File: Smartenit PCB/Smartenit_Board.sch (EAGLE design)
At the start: 86 parts, among them J1 2X5CONNECTOR1.27MM, Q1 QUARTZ_3.58M_2PIN, U1 SN74LVC1G3157, U2 ADE7953, U3 ESP-WROOM-32

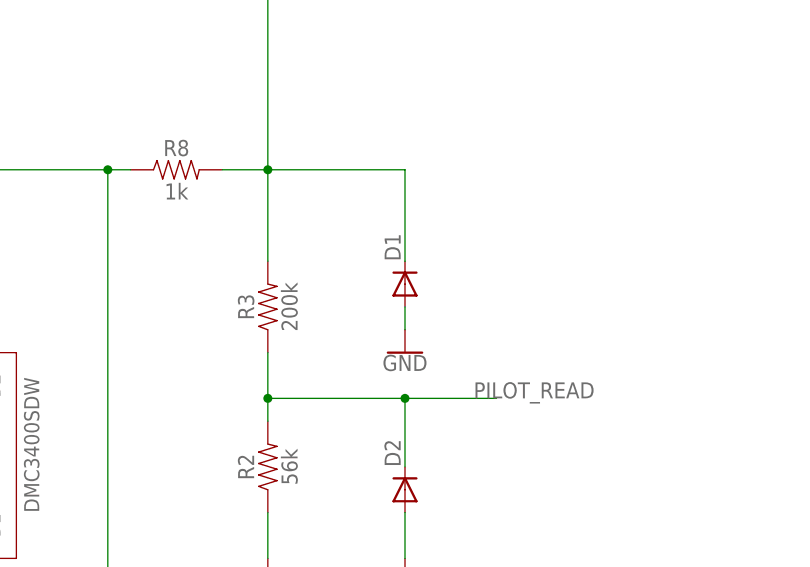
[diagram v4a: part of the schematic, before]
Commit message: fixed diodes
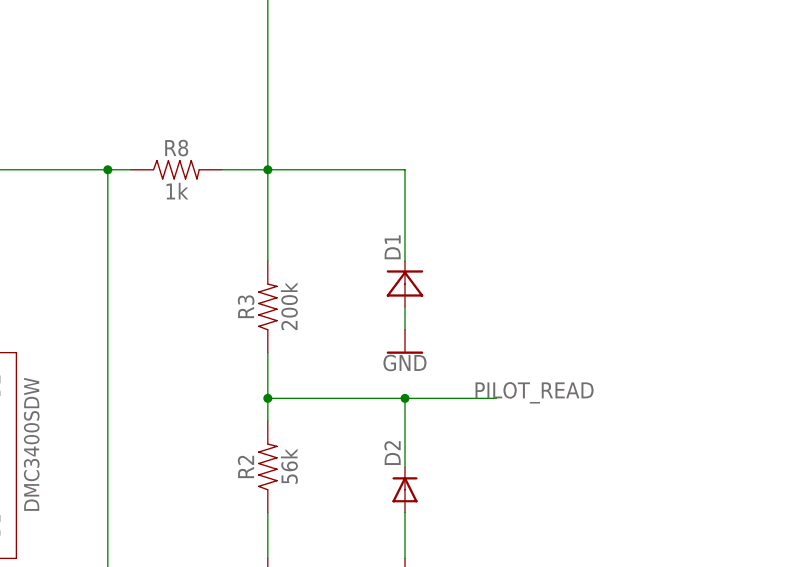
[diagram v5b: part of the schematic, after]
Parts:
- D1: device diode:DIODE-SMB -> Smart_Charger:TVSDIODE
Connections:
- net DGND: now also D1.P; no longer D1.A
- net PILOT: now also D1.N; no longer D1.C
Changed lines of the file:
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@@
 <grid distance="0.1" unitdist="inch" unit="inch" style="lines" multiple="1" display="no" altdistance="0.01" altunitdist="inch" altunit="inch"/>
 <layers>
-<layer number="1" name="Top" color="4" fill="1" visible="no" active="no"/>
-<layer number="2" name="Route2" color="1" fill="3" visible="no" active="no"/>
-<layer number="3" name="Route3" color="4" fill="3" visible="no" active="no"/>
-<layer number="4" name="Route4" color="1" fill="4" visible="no" active="no"/>
-<layer number="5" name="Route5" color="4" fill="4" visible="no" active="no"/>
-<layer number="6" name="Route6" color="1" fill="8" visible="no" active="no"/>
-<layer number="7" name="Route7" color="4" fill="8" visible="no" active="no"/>
-<layer number="8" name="Route8" color="1" fill="2" visible="no" active="no"/>
-<layer number="9" name="Route9" color="4" fill="2" visible="no" active="no"/>
-<layer number="10" name="Route10" color="1" fill="7" visible="no" active="no"/>
-<layer number="11" name="Route11" color="4" fill="7" visible="no" active="no"/>
-<layer number="12" name="Route12" color="1" fill="5" visible="no" active="no"/>
-<layer number="13" name="Route13" color="4" fill="5" visible="no" active="no"/>
-<layer number="14" name="Route14" color="1" fill="6" visible="no" active="no"/>
-<layer number="15" name="Route15" color="4" fill="6" visible="no" active="no"/>
-<layer number="16" name="Bottom" color="1" fill="1" visible="no" active="no"/>
-<layer number="17" name="Pads" color="2" fill="1" visible="no" active="no"/>
-<layer number="18" name="Vias" color="2" fill="1" visible="no" active="no"/>
-<layer number="19" name="Unrouted" color="6" fill="1" visible="no" active="no"/>
-<layer number="20" name="Dimension" color="15" fill="1" visible="no" active="no"/>
-<layer number="21" name="tPlace" color="7" fill="1" visible="no" active="no"/>
-<layer number="22" name="bPlace" color="7" fill="1" visible="no" active="no"/>
-<layer number="23" name="tOrigins" color="15" fill="1" visible="no" active="no"/>
-<layer number="24" name="bOrigins" color="15" fill="1" visible="no" active="no"/>
-<layer number="25" name="tNames" color="7" fill="1" visible="no" active="no"/>
-<layer number="26" name="bNames" color="7" fill="1" visible="no" active="no"/>
-<layer number="27" name="tValues" color="7" fill="1" visible="no" active="no"/>
-<layer number="28" name="bValues" color="7" fill="1" visible="no" active="no"/>
+<layer number="1" name="Top" color="4" fill="1" visible="yes" active="no"/>
+<layer number="2" name="Route2" color="1" fill="3" visible="yes" active="no"/>
+<layer number="3" name="Route3" color="4" fill="3" visible="yes" active="no"/>
+<layer number="4" name="Route4" color="1" fill="4" visible="yes" active="no"/>
+<layer number="5" name="Route5" color="4" fill="4" visible="yes" active="no"/>
+<layer number="6" name="Route6" color="1" fill="8" visible="yes" active="no"/>
+<layer number="7" name="Route7" color="4" fill="8" visible="yes" active="no"/>
+<layer number="8" name="Route8" color="1" fill="2" visible="yes" active="no"/>
+<layer number="9" name="Route9" color="4" fill="2" visible="yes" active="no"/>
+<layer number="10" name="Route10" color="1" fill="7" visible="yes" active="no"/>
+<layer number="11" name="Route11" color="4" fill="7" visible="yes" active="no"/>
+<layer number="12" name="Route12" color="1" fill="5" visible="yes" active="no"/>
+<layer number="13" name="Route13" color="4" fill="5" visible="yes" active="no"/>
+<layer number="14" name="Route14" color="1" fill="6" visible="yes" active="no"/>
+<layer number="15" name="Route15" color="4" fill="6" visible="yes" active="no"/>
+<layer number="16" name="Bottom" color="1" fill="1" visible="yes" active="no"/>
+<layer number="17" name="Pads" color="2" fill="1" visible="yes" active="no"/>
+<layer number="18" name="Vias" color="2" fill="1" visible="yes" active="no"/>
+<layer number="19" name="Unrouted" color="6" fill="1" visible="yes" active="no"/>
+<layer number="20" name="Dimension" color="15" fill="1" visible="yes" active="no"/>
+<layer number="21" name="tPlace" color="7" fill="1" visible="yes" active="no"/>
+<layer number="22" name="bPlace" color="7" fill="1" visible="yes" active="no"/>
+<layer number="23" name="tOrigins" color="15" fill="1" visible="yes" active="no"/>
+<layer number="24" name="bOrigins" color="15" fill="1" visible="yes" active="no"/>
+<layer number="25" name="tNames" color="7" fill="1" visible="yes" active="no"/>
+<layer number="26" name="bNames" color="7" fill="1" visible="yes" active="no"/>
+<layer number="27" name="tValues" color="7" fill="1" visible="yes" active="no"/>
+<layer number="28" name="bValues" color="7" fill="1" visible="yes" active="no"/>
 <layer number="29" name="tStop" color="7" fill="3" visible="no" active="no"/>
 <layer number="30" name="bStop" color="7" fill="6" visible="no" active="no"/>
@@
 <layer number="35" name="tGlue" color="7" fill="4" visible="no" active="no"/>
 <layer number="36" name="bGlue" color="7" fill="5" visible="no" active="no"/>
-<layer number="37" name="tTest" color="7" fill="1" visible="no" active="no"/>
-<layer number="38" name="bTest" color="7" fill="1" visible="no" active="no"/>
+<layer number="37" name="tTest" color="7" fill="1" visible="yes" active="no"/>
+<layer number="38" name="bTest" color="7" fill="1" visible="yes" active="no"/>
 <layer number="39" name="tKeepout" color="4" fill="11" visible="no" active="no"/>
 <layer number="40" name="bKeepout" color="1" fill="11" visible="no" active="no"/>
@@
 <layer number="44" name="Drills" color="7" fill="1" visible="no" active="no"/>
 <layer number="45" name="Holes" color="7" fill="1" visible="no" active="no"/>
-<layer number="46" name="Milling" color="3" fill="1" visible="no" active="no"/>
-<layer number="47" name="Measures" color="7" fill="1" visible="no" active="no"/>
-<layer number="48" name="Document" color="7" fill="1" visible="no" active="no"/>
-<layer number="49" name="Reference" color="14" fill="1" visible="no" active="no"/>
-<layer number="50" name="dxf" color="7" fill="1" visible="no" active="no"/>
-<layer number="51" name="tDocu" color="6" fill="1" visible="no" active="no"/>
-<layer number="52" name="bDocu" color="6" fill="1" visible="no" active="no"/>
-<layer number="53" name="tGND_GNDA" color="7" fill="9" visible="no" active="no"/>
-<layer number="54" name="bGND_GNDA" color="1" fill="9" visible="no" active="no"/>
-<layer number="56" name="wert" color="7" fill="1" visible="no" active="no"/>
-<layer number="57" name="tCAD" color="7" fill="1" visible="no" active="no"/>
-<layer number="59" name="tCarbon" color="7" fill="1" visible="no" active="no"/>
-<layer number="60" name="bCarbon" color="7" fill="1" visible="no" active="no"/>
+<layer number="46" name="Milling" color="3" fill="1" visible="yes" active="no"/>
+<layer number="47" name="Measures" color="7" fill="1" visible="yes" active="no"/>
+<layer number="48" name="Document" color="7" fill="1" visible="yes" active="no"/>
+<layer number="49" name="Reference" color="14" fill="1" visible="yes" active="no"/>
+<layer number="50" name="dxf" color="7" fill="1" visible="yes" active="no"/>
+<layer number="51" name="tDocu" color="6" fill="1" visible="yes" active="no"/>
+<layer number="52" name="bDocu" color="6" fill="1" visible="yes" active="no"/>
+<layer number="53" name="tGND_GNDA" color="7" fill="9" visible="yes" active="no"/>
+<layer number="54" name="bGND_GNDA" color="1" fill="9" visible="yes" active="no"/>
+<layer number="56" name="wert" color="7" fill="1" visible="yes" active="no"/>
+<layer number="57" name="tCAD" color="7" fill="1" visible="yes" active="no"/>
+<layer number="59" name="tCarbon" color="7" fill="1" visible="yes" active="no"/>
+<layer number="60" name="bCarbon" color="7" fill="1" visible="yes" active="no"/>
 <layer number="88" name="SimResults" color="9" fill="1" visible="no" active="yes"/>
 <layer number="89" name="SimProbes" color="9" fill="1" visible="no" active="yes"/>
@@
 <part name="GNDI30" library="SparkFun" deviceset="GND" device=""/>
 <part name="D3" library="Smart_Charger" deviceset="SS32_DIODE" device=""/>
-<part name="D1" library="diode" library_urn="urn:adsk.eagle:library:210" deviceset="DIODE-" device="SMB" package3d_urn="urn:adsk.eagle:package:43404/2" value="P6SMB16A"/>
+<part name="D1" library="Smart_Charger" deviceset="TVSDIODE" device="" value="P6SMB16A"/>
 </parts>
 <sheets>
@@
 <wire x1="-236.22" y1="203.2" x2="-226.06" y2="203.2" width="0.1524" layer="91"/>
 <label x="-231.14" y="203.2" size="1.778" layer="95"/>
-<pinref part="D1" gate="G$1" pin="C"/>
+<pinref part="D1" gate="G$1" pin="N"/>
 </segment>
 </net>
@@
 <pinref part="GND5" gate="1" pin="GND"/>
 <wire x1="-220.98" y1="162.56" x2="-220.98" y2="165.1" width="0.1524" layer="91"/>
-<pinref part="D1" gate="G$1" pin="A"/>
-</segment>
-<segment>
+<pinref part="D1" gate="G$1" pin="P"/>
+</segment>
+<segment>

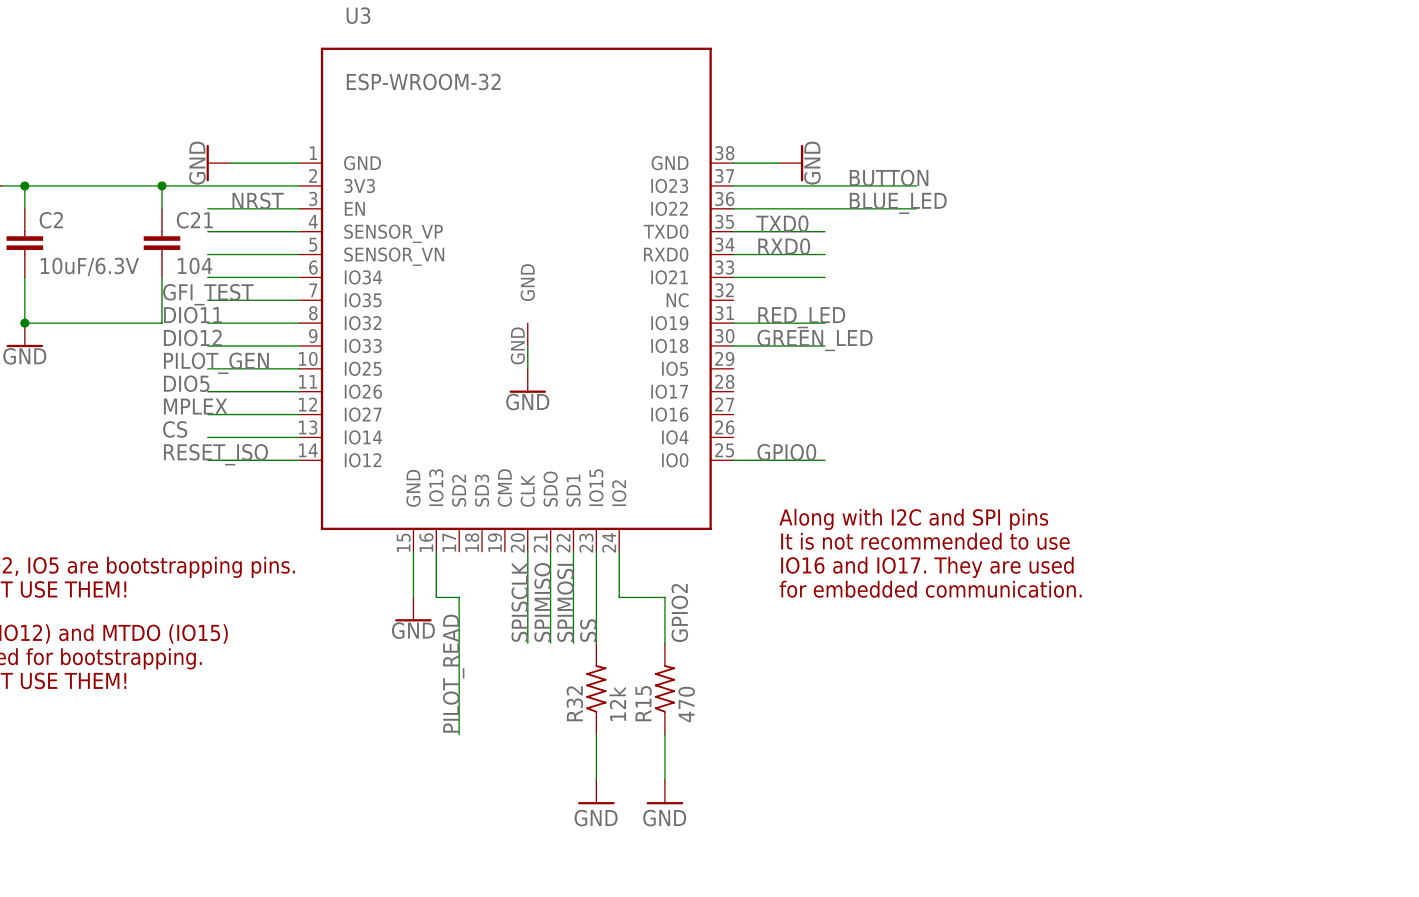
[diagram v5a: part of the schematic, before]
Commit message: Rerouting for new pins
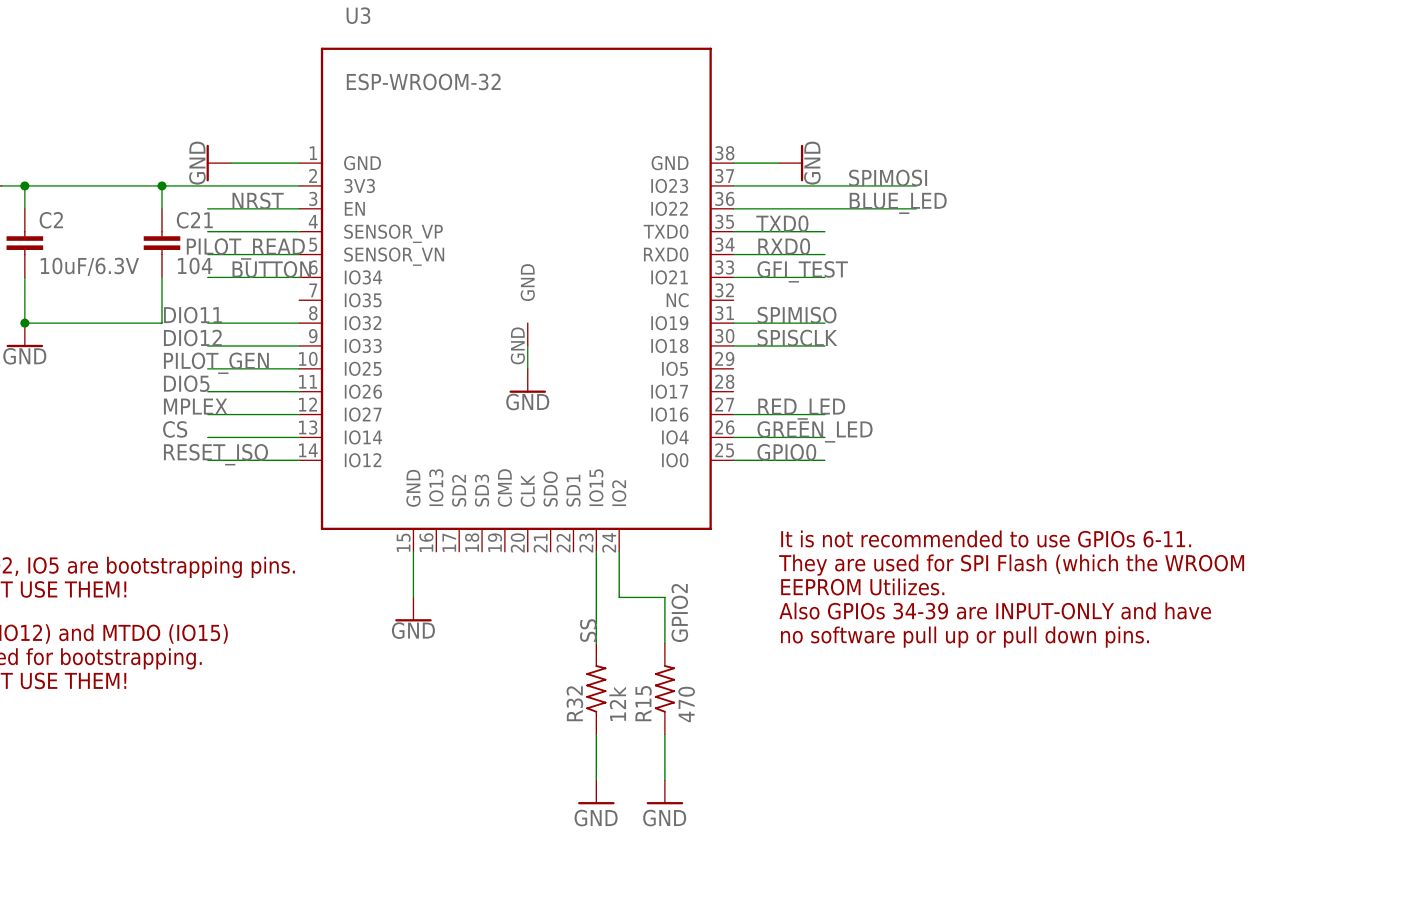
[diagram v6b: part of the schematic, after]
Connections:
- removed net N$45: U3.IO34
- removed net N$46: U3.SENSOR_VN
- removed net N$53: U3.IO21
- net BUTTON: now also U3.IO34; no longer U3.IO23
- net GFI_TEST: now also U3.IO21; no longer U3.IO35
- net GREEN_LED: now also U3.IO4; no longer U3.IO18
- net PILOT_READ: now also U3.SENSOR_VN; no longer U3.IO13
- net RED_LED: now also U3.IO16; no longer U3.IO19
- net SPIMISO: now also U3.IO19; no longer U3.SDO
- net SPIMOSI: now also U3.IO23; no longer U3.SD1
- net SPISCLK: now also U3.IO18; no longer U3.CLK
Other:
- note added: "It is not recommended to use GPIOs 6-11. They are used for SPI Flash (which the WROOM EEPROM Utilizes. Also GPIOs 34-39 are INPUT-ONLY and have no software pull up or pull down pins."
- note removed: "Along with I2C and SPI pins It is not recommended to use IO16 and IO17. They are used for embedded communication."
